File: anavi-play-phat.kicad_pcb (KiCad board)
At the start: 2 copper layers, 65 x 30 mm, 25 parts, among them U1 CAT24C32WI-GT3

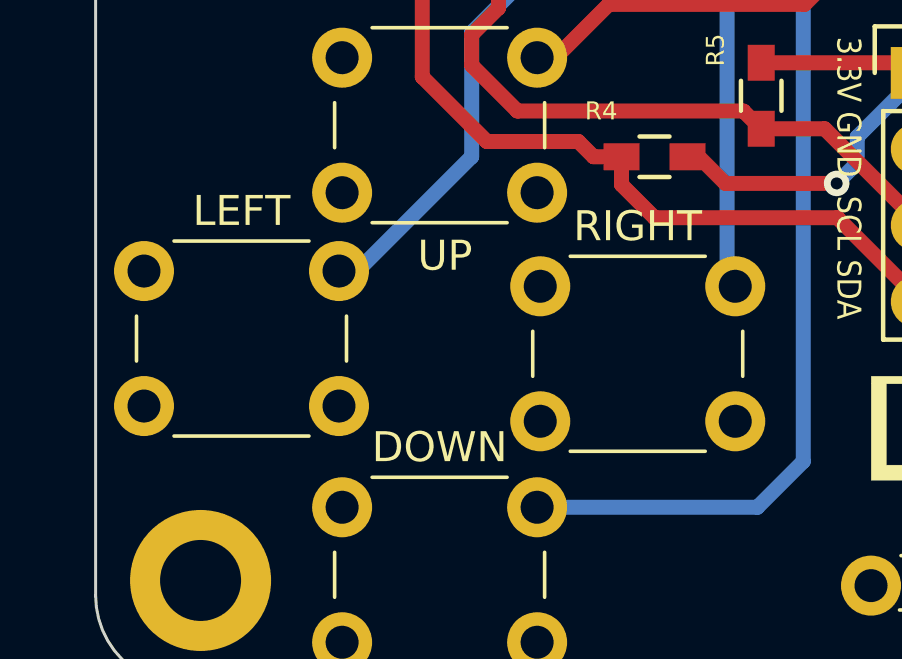
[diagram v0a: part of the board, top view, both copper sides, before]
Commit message: anavi-play-phat.kicad_pcb: Update arrows
Signed-off-by: Leon Anavi <leon@anavi.org>
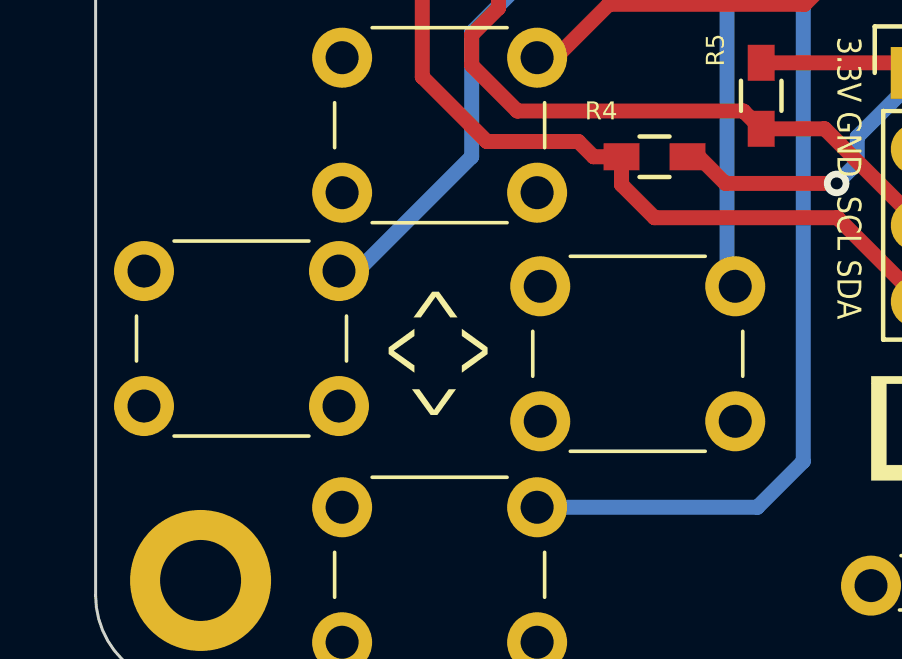
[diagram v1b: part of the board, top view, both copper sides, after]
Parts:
- renumbered LEFT to <, DOWN to <, RIGHT to >, UP to >
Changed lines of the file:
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@@
   )
   (layers
-    (0 F.Cu signal hide)
+    (0 F.Cu signal)
     (31 B.Cu signal)
     (32 B.Adhes user)
@@
     (descr "tactile push button, 6x6mm e.g. PHAP33xx series, height=4.3mm")
     (tags "tact sw push 6mm")
-    (fp_text reference LEFT (at 3.25 -2) (layer F.SilkS)
-      (effects (font (size 1 1) (thickness 0.15)))
+    (fp_text reference < (at 8.5852 2.5908) (layer F.SilkS)
+      (effects (font (size 2 1) (thickness 0.2)))
     )
     (fp_text value SW_DIP_x01 (at 3.75 6.7) (layer F.Fab) hide
       (effects (font (size 1 1) (thickness 0.15)))
     )
-    (fp_text user %R (at 3.25 2.25) (layer F.Fab)
+    (fp_text user %R (at 3.25 2.25) (layer F.Fab) hide
       (effects (font (size 1 1) (thickness 0.15)))
     )
@@
     (descr "tactile push button, 6x6mm e.g. PHAP33xx series, height=4.3mm")
     (tags "tact sw push 6mm")
-    (fp_text reference RIGHT (at 3.25 -2) (layer F.SilkS)
-      (effects (font (size 1 1) (thickness 0.15)))
+    (fp_text reference > (at -2.1844 2.0828) (layer F.SilkS)
+      (effects (font (size 2 1) (thickness 0.25)))
     )
     (fp_text value SW_DIP_x01 (at 3.75 6.7) (layer F.Fab) hide
       (effects (font (size 1 1) (thickness 0.15)))
     )
-    (fp_text user %R (at 3.25 2.25) (layer F.Fab)
+    (fp_text user %R (at 3.25 2.25) (layer F.Fab) hide
       (effects (font (size 1 1) (thickness 0.15)))
     )
@@
     (descr "tactile push button, 6x6mm e.g. PHAP33xx series, height=4.3mm")
     (tags "tact sw push 6mm")
-    (fp_text reference UP (at 3.429 6.604) (layer F.SilkS)
-      (effects (font (size 1 1) (thickness 0.15)))
+    (fp_text reference > (at 3.048 8.2296 90) (layer F.SilkS)
+      (effects (font (size 2 1) (thickness 0.25)))
     )
     (fp_text value SW_DIP_x01 (at 3.75 6.7) (layer F.Fab) hide
       (effects (font (size 1 1) (thickness 0.15)))
     )
-    (fp_text user %R (at 3.25 2.25) (layer F.Fab)
+    (fp_text user %R (at 3.25 2.25) (layer F.Fab) hide
       (effects (font (size 1 1) (thickness 0.15)))
     )
@@
     (descr "tactile push button, 6x6mm e.g. PHAP33xx series, height=4.3mm")
     (tags "tact sw push 6mm")
-    (fp_text reference DOWN (at 3.25 -2) (layer F.SilkS)
-      (effects (font (size 1 1) (thickness 0.15)))
+    (fp_text reference < (at 2.9972 -3.5052 90) (layer F.SilkS)
+      (effects (font (size 2 1) (thickness 0.25)))
     )
     (fp_text value SW_DIP_x01 (at 3.75 6.7) (layer F.Fab) hide
       (effects (font (size 1 1) (thickness 0.15)))
     )
-    (fp_text user %R (at 3.25 2.25) (layer F.Fab)
-      (effects (font (size 1 1) (thickness 0.15)))
-    )
+    (fp_text user %R (at 3.25 2.25) (layer F.Fab) hide
+      (effects (font (size 1 1) (thickness 0.15)))
+    )
